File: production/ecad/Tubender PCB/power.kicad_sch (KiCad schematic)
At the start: 38 parts, among them Q1 CSD19502Q5B, Q2 CSD19534Q5A, U1 LMR36520FADDAR, U2 LM5146RGYR, U3 TPSM265R1V5SILR

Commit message: STATUS LEDS!!!
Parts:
- added D_IND12, D_IND3, D_IND48, D_IND5: WL-SMCW_0603, WL-SMCW_0603:WL-SMCW_0603, symbol WL-SMCW_0603:WL-SMCW_0603
- added R_IND12: 280, symbol Device:R_Small_US
- added R_IND3: 3.4, symbol Device:R_Small_US
- added R_IND48: 1.2k, symbol Device:R_Small_US
- added R_IND5: 60, symbol Device:R_Small_US
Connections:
- net +48V: now also R_IND48.1
- net 12V: now also R_IND12.1
- net 3V3: now also R_IND3.1
- net 5V: now also R_IND5.1
- net GND: now also D_IND12.1, D_IND3.1, D_IND48.1, D_IND5.1
- new net: D_IND12.2, R_IND12.2
- new net: D_IND3.2, R_IND3.2
- new net: D_IND5.2, R_IND5.2
- new net: D_IND48.2, R_IND48.2
- no-connect marks 5 -> 4
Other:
- note added: "STATUS LEDS!!!!!!"

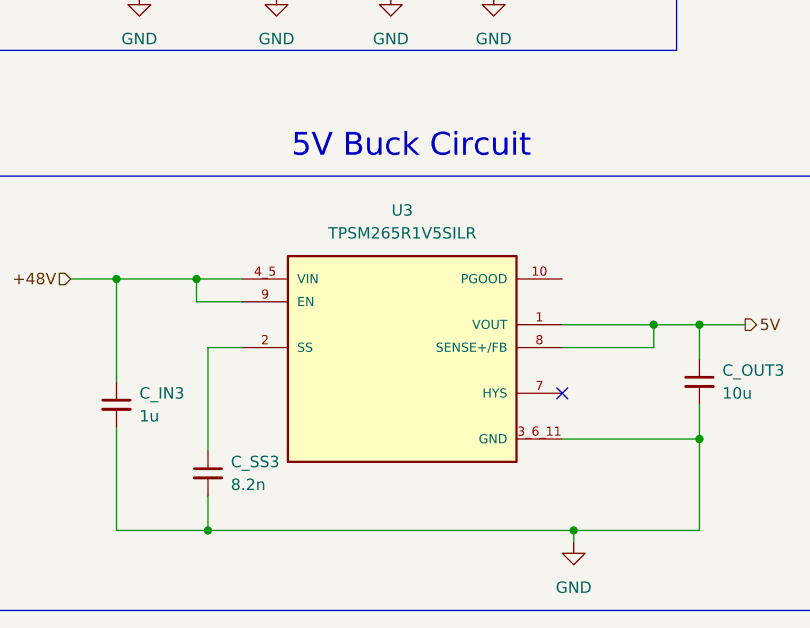
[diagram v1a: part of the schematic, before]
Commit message: 7 Segment, Buttons, Plexers Oh MY!
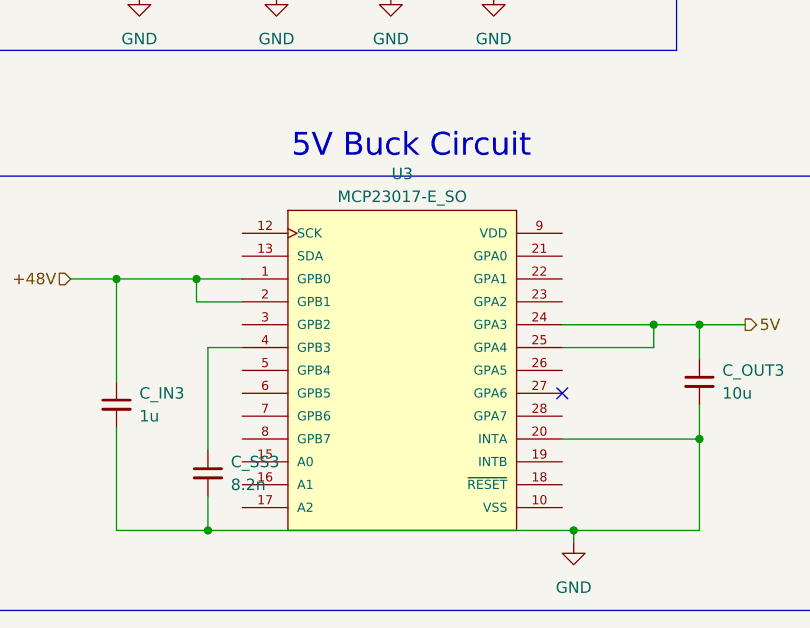
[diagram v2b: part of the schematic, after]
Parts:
- U3: value TPSM265R1V5SILR -> MCP23017-E_SO; footprint TPSM265R1V5SILR:CONV_TPSM265R1V5SILR -> MCP23017-E_SO:SOIC127P1030X265-28N; A1_MIN (none) -> 0.1; A_MAX (none) -> 2.65; A_MIN (none) -> 2.65; A_NOM (none) -> 2.65; B_MAX (none) -> 0.51; B_MIN (none) -> 0.31; B_NOM (none) -> 0.41; D2_MAX (none) -> 0.0; D_MAX (none) -> 17.9; D_MIN (none) -> 17.9; D_NOM (none) -> 17.9; E1_MAX (none) -> 7.5; E1_MIN (none) -> 7.5; E1_NOM (none) -> 7.5; E2_MAX (none) -> 0.0; ENOM (none) -> 1.27; E_MAX (none) -> 10.3; E_MIN (none) -> 10.3; E_NOM (none) -> 10.3; L_MAX (none) -> 1.27; L_MIN (none) -> 0.4; L_NOM (none) -> 0.835; MANUFACTURER Texas Instruments -> Microchip; MAXIMUM_PACKAGE_HEIGHT 1.9mm -> 2.65mm; PARTREV B -> C; PIN_COUNT (none) -> 28.0; STANDARD Manufacturer Recommendations -> IPC 7351B
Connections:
- net +48V: now also U3.1 (GPB0), U3.2 (GPB1); no longer U3.4_5 (VIN), U3.9 (EN)
- net 5V: now also U3.24 (GPA3), U3.25 (GPA4); no longer U3.1 (VOUT), U3.8 (SENSE+/FB)
- net GND: now also U3.20 (INTA); no longer U3.3_6_11 (GND)
- net at C_SS3.1: now also U3.4 (GPB3); no longer U3.2 (SS)

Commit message: Formatting
Boom
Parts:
- renumbered U2 to U11
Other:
- moved on the sheet: CBOOT1, CIN1, C_BST2, C_C1, C_C2, C_C3, C_HF1, C_ILIM, C_IN2, C_IN3, C_OUT1, C_OUT2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

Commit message: 24V Buck Said WHOOO?!
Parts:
- added C14, C16: 1uF, symbol Device:C
- added C15: 10nF, symbol Device:C
- added R43: 56.2k, symbol Device:R_US
- added R44: 2k, symbol Device:R_US
- added R45: 681k, symbol Device:R_US
- added U13: LM5017SDX/NOPB, SDC08B, symbol 2024-10-11_02-12-55:LM5017SDX_NOPB
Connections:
- net +48V: now also C14.1, R43.2, R45.2, U13.2 (VIN)
- net GND: now also C14.2, C16.2, R44.1, U13.1 (RTN)
- new net: R43.1, R44.2, U13.3 (UVLO)
- new net: R45.1, U13.4 (RON)
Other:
- note added: "24V Buck Circuit"
- moved on the sheet: CBOOT1, CIN1, C_BST2, C_C1, C_C2, C_C3, C_HF1, C_ILIM, C_IN2, C_IN3, C_OUT1, C_OUT2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

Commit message: adjustments
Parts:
- added C17: 10uF, symbol Device:C
- added D_IND1: WL-SMCW_0603, WL-SMCW_0603:WL-SMCW_0603, symbol WL-SMCW_0603:WL-SMCW_0603
- added L3: 220uH, symbol Device:L
- added R46: 10k, symbol Device:R_US
- added R47: 549, symbol Device:R_US
- added R48: 250m, symbol Device:R_US
- added R_IND1: 600, symbol Device:R_Small_US
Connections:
- net GND: now also D_IND1.1, R47.1, R48.1
- net at C16.1: now also U13.6 (VCC)
- net at U13.5 (FB): now also R46.1, R47.2
- net at U13.7 (BST): now also C15.1
- net at U13.8 (SW): now also C15.2, L3.1
- new net: C17.2, R48.2
- new net: D_IND1.2, R_IND1.2
- new net +24V: R_IND1.1
- new net 24V: C17.1, L3.2, R46.2
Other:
- moved on the sheet: C14, C15, C16, D_IND12, D_IND3, D_IND48, D_IND5, R43, R44, R45, R_IND12, R_IND3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

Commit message: Fixed Button Connectors
All done! Enjoy :)
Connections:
- net +24V is gone; now on net 24V: R_IND1.1
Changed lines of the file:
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@@
 		)
 	)
-	(hierarchical_label "+24V"
+	(hierarchical_label "24V"
 		(shape input)
 		(at 175.26 139.7 90)

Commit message: Fixed 12V buck and power LEDs
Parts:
- added R_VIN12: 2.2, symbol Device:R_Small_US
- R_ILIM: value 1k -> 1.58k
- R_IND12: value 280 -> 340
- R_IND48: value 1.2k -> 1.5k
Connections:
- net +48V: now also R_VIN12.1
- net GND: now also Q2.1 (S), Q2.2 (S), Q2.3 (S)
- net at C_VIN1.1, R_UV1.1, U11.20 (VIN): now also R_VIN12.2
- net at C_C2.2, C_C3.2, R_C1.2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: no longer Q2.1 (S), Q2.2 (S), Q2.3 (S)
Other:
- moved on the sheet: C_ILIM, Q2, R_ILIM
